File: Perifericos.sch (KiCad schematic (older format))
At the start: 26 parts, among them IC2 TLE493DW2B6A2HTSA1

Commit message: Update+UL PCB
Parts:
- FLASH_MEM1: value W25Q32JVZP -> W25Q64JWZPIM
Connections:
- net FLASH_CLK: no longer PINS_IZQ1.13 (Pin_13)
- net FLASH_SDI: no longer PINS_DER1.12 (Pin_12)
- net FLASH_SDO: no longer PINS_DER1.14 (Pin_14)
- net FLASH_nCS: no longer PINS_DER1.5 (Pin_5)
- net GND: now also BTN_RST1.1; no longer BTN_RST1.2
- net VDDS: now also C110.1, Giroscope1.8 (VDDIO)
- net at R_RESET1.2: now also BTN_RST1.2; no longer BTN_RST1.1
- net GPIO18: no longer names the net of PINS_DER1.9 (Pin_9)
- net GPIO19: no longer names the net of PINS_DER1.7 (Pin_7)
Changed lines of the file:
@@
 P 1900 5850
 F 0 "FLASH_MEM1" H 2300 6600 50  0000 C CNN
-F 1 "W25Q32JVZP" H 2350 6400 50  0000 C CNN
+F 1 "W25Q64JWZPIM" H 2350 6400 50  0000 C CNN
 F 2 "Package_SON:WSON-8-1EP_6x5mm_P1.27mm_EP3.4x4.3mm" H 1900 5850 50  0001 C CNN
 F 3 "http://www.winbond.com/resource-files/w25q32jv%20revg%2003272018%20plus.pdf" H 1900 5850 50  0001 C CNN
@@
 Text GLabel 5100 4350 0    50   Input ~ 0
 GPIO24
-Text GLabel 5100 4450 0    50   Input ~ 0
-GPIO10
 Text GLabel 5100 4550 0    50   Input ~ 0
 GPIO21
@@
 Text GLabel 7350 3950 0    50   Input ~ 0
 GPIO6
-Text GLabel 7350 4050 0    50   Input ~ 0
-GPIO20
-Text GLabel 7350 4150 0    50   Input ~ 0
-GPIO19
-Text GLabel 7350 4250 0    50   Input ~ 0
-GPIO18
 Text GLabel 7350 4450 0    50   Input ~ 0
 JTAG_TMSC
@@
 Text GLabel 7850 4250 2    50   Input ~ 0
 RESET_N
-Text GLabel 7850 4350 2    50   Input ~ 0
-GPIO9
-Text GLabel 7850 4450 2    50   Input ~ 0
-GPIO8
 Text GLabel 7850 4550 2    50   Input ~ 0
 GPIO13
@@
 F 3 "https://www.mouser.ca/c/?q=pts645" H 5250 6900 50  0001 C CNN
 	1    5250 6900
-	0    1    1    0
+	0    -1   -1   0
 $EndComp
 $Comp
@@
 Wire Wire Line
 	1350 7300 1100 7300
-Text GLabel 1350 7450 2    50   Input ~ 0
+Text GLabel 1350 7600 2    50   Input ~ 0
 GPIO10
 Text GLabel 1350 7750 2    50   Input ~ 0
 GPIO8
-Text GLabel 1350 7600 2    50   Input ~ 0
+Text GLabel 1350 7450 2    50   Input ~ 0
 GPIO9
 Wire Wire Line
@@
 	10400 4900 10400 4800
 Connection ~ 10400 4800
+Text GLabel 1950 2600 1    50   Input ~ 0
+VDDS
 $EndSCHEMATC

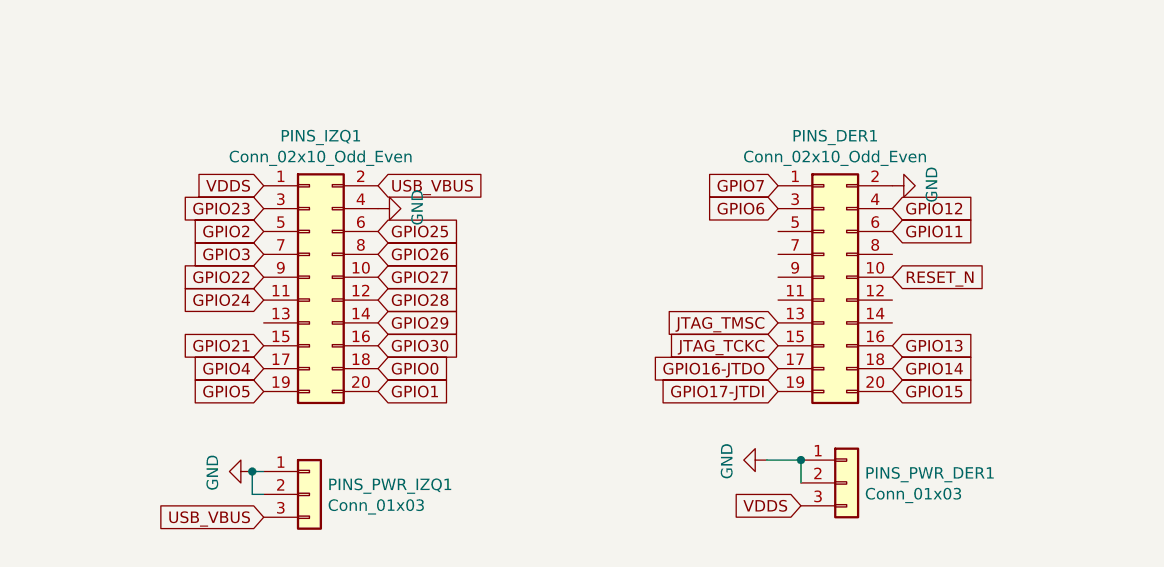
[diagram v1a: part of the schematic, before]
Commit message: V2 PIN Route
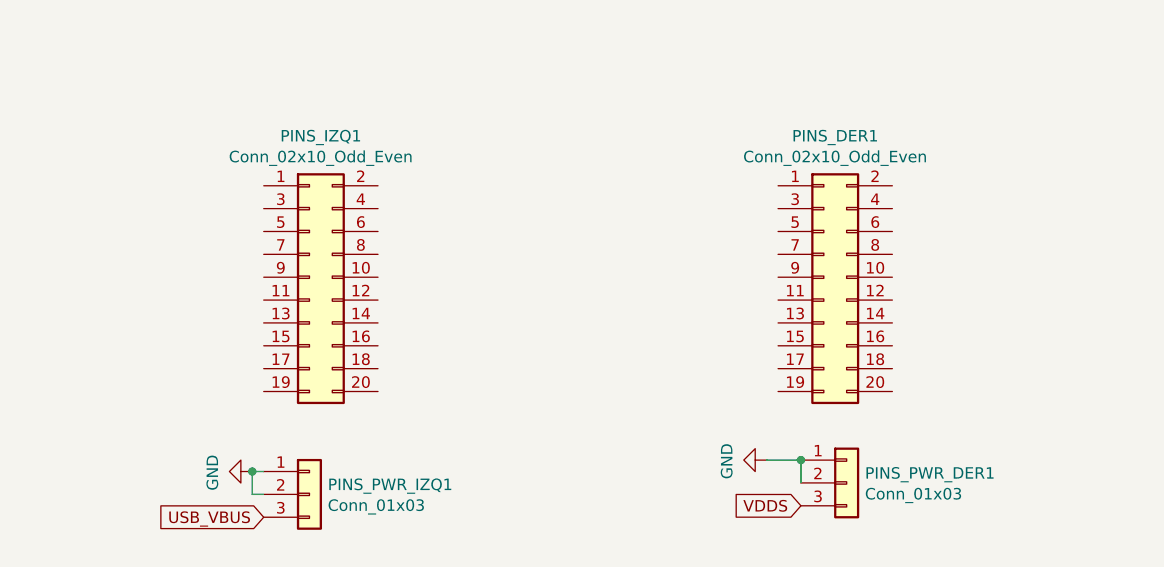
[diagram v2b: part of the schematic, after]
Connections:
- net GND: no longer PINS_DER1.2 (Pin_2), PINS_IZQ1.4 (Pin_4)
- net GPIO13: no longer PINS_DER1.16 (Pin_16)
- net GPIO14: no longer PINS_DER1.18 (Pin_18)
- net GPIO24: no longer PINS_IZQ1.11 (Pin_11)
- net GPIO25: no longer PINS_IZQ1.6 (Pin_6)
- net GPIO26: no longer PINS_IZQ1.8 (Pin_8)
- net GPIO6: no longer PINS_DER1.3 (Pin_3)
- net GPIO7: no longer PINS_DER1.1 (Pin_1)
- net RESET_N: no longer PINS_DER1.10 (Pin_10)
- net USB_VBUS: no longer PINS_IZQ1.2 (Pin_2)
- net VDDS: no longer PINS_IZQ1.1 (Pin_1)
- net GPIO0: no longer names the net of PINS_IZQ1.18 (Pin_18)
- net GPIO1: no longer names the net of PINS_IZQ1.20 (Pin_20)
- net GPIO11: no longer names the net of PINS_DER1.6 (Pin_6)
- net GPIO12: no longer names the net of PINS_DER1.4 (Pin_4)
- net GPIO15: no longer names the net of PINS_DER1.20 (Pin_20)
- net GPIO16-JTDO: no longer names the net of PINS_DER1.17 (Pin_17)
- net GPIO17-JTDI: no longer names the net of PINS_DER1.19 (Pin_19)
- net GPIO2: no longer names the net of PINS_IZQ1.5 (Pin_5)
- net GPIO21: no longer names the net of PINS_IZQ1.15 (Pin_15)
- net GPIO22: no longer names the net of PINS_IZQ1.9 (Pin_9)
- net GPIO23: no longer names the net of PINS_IZQ1.3 (Pin_3)
- net GPIO27: no longer names the net of PINS_IZQ1.10 (Pin_10)
- net GPIO28: no longer names the net of PINS_IZQ1.12 (Pin_12)
- net GPIO29: no longer names the net of PINS_IZQ1.14 (Pin_14)
- net GPIO3: no longer names the net of PINS_IZQ1.7 (Pin_7)
- net GPIO30: no longer names the net of PINS_IZQ1.16 (Pin_16)
- net GPIO4: no longer names the net of PINS_IZQ1.17 (Pin_17)
- net GPIO5: no longer names the net of PINS_IZQ1.19 (Pin_19)
- net JTAG_TCKC: no longer names the net of PINS_DER1.15 (Pin_15)
- net JTAG_TMSC: no longer names the net of PINS_DER1.13 (Pin_13)
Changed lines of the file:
@@
 	1    0    0    -1
 $EndComp
-Text GLabel 5100 3850 0    50   Input ~ 0
-VDDS
-Text GLabel 5600 3850 2    50   Input ~ 0
-USB_VBUS
-$Comp
-L power:GND #PWR?
-U 1 1 6113ADAF
-P 5600 3950
-AR Path="/6113ADAF" Ref="#PWR?"  Part="1"
-AR Path="/610C2981/6113ADAF" Ref="#PWR0133"  Part="1"
-F 0 "#PWR0133" H 5600 3700 50  0001 C CNN
-F 1 "GND" H 5605 3777 50  0000 C CNN
-F 2 "" H 5600 3950 50  0001 C CNN
-F 3 "" H 5600 3950 50  0001 C CNN
-	1    5600 3950
-	0    -1   -1   0
-$EndComp
-Text GLabel 5100 3950 0    50   Input ~ 0
-GPIO23
-Text GLabel 5100 4050 0    50   Input ~ 0
-GPIO2
-Text GLabel 5100 4150 0    50   Input ~ 0
-GPIO3
-Text GLabel 5100 4250 0    50   Input ~ 0
-GPIO22
-Text GLabel 5100 4350 0    50   Input ~ 0
-GPIO24
-Text GLabel 5100 4550 0    50   Input ~ 0
-GPIO21
-Text GLabel 5100 4650 0    50   Input ~ 0
-GPIO4
-Text GLabel 5100 4750 0    50   Input ~ 0
-GPIO5
-Text GLabel 5600 4050 2    50   Input ~ 0
-GPIO25
-Text GLabel 5600 4150 2    50   Input ~ 0
-GPIO26
-Text GLabel 5600 4250 2    50   Input ~ 0
-GPIO27
-Text GLabel 5600 4350 2    50   Input ~ 0
-GPIO28
-Text GLabel 5600 4450 2    50   Input ~ 0
-GPIO29
-Text GLabel 5600 4550 2    50   Input ~ 0
-GPIO30
-Text GLabel 5600 4650 2    50   Input ~ 0
-GPIO0
-Text GLabel 5600 4750 2    50   Input ~ 0
-GPIO1
-$Comp
-L power:GND #PWR?
-U 1 1 6113CE9D
-P 7850 3850
-AR Path="/6113CE9D" Ref="#PWR?"  Part="1"
-AR Path="/610C2981/6113CE9D" Ref="#PWR0134"  Part="1"
-F 0 "#PWR0134" H 7850 3600 50  0001 C CNN
-F 1 "GND" H 7855 3677 50  0000 C CNN
-F 2 "" H 7850 3850 50  0001 C CNN
-F 3 "" H 7850 3850 50  0001 C CNN
-	1    7850 3850
-	0    -1   -1   0
-$EndComp
-Text GLabel 7350 3850 0    50   Input ~ 0
-GPIO7
-Text GLabel 7350 3950 0    50   Input ~ 0
-GPIO6
-Text GLabel 7350 4450 0    50   Input ~ 0
-JTAG_TMSC
-Text GLabel 7350 4550 0    50   Input ~ 0
-JTAG_TCKC
-Text GLabel 7350 4650 0    50   Input ~ 0
-GPIO16-JTDO
-Text GLabel 7350 4750 0    50   Input ~ 0
-GPIO17-JTDI
-Text GLabel 7850 3950 2    50   Input ~ 0
-GPIO12
-Text GLabel 7850 4050 2    50   Input ~ 0
-GPIO11
-Text GLabel 7850 4250 2    50   Input ~ 0
-RESET_N
-Text GLabel 7850 4550 2    50   Input ~ 0
-GPIO13
-Text GLabel 7850 4650 2    50   Input ~ 0
-GPIO14
-Text GLabel 7850 4750 2    50   Input ~ 0
-GPIO15
 $Comp
 L Connector_Generic:Conn_01x03 PINS_PWR_IZQ1
